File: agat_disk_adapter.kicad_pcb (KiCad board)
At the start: 2 copper layers, 58.4 x 63.5 mm, 14 parts, among them J1 КОНТРОЛЛЕР, J2_A1 ИЗОТ, J2_B2 ИЗОТ, J3 DISK II, J4 GOTEK, J5 Питание GOTEK, J6 ВБ, J7 Джамперы, J8 ВБ2, J9_A1 КОНТРОЛЛЕР, J9_B2 КОНТРОЛЛЕР

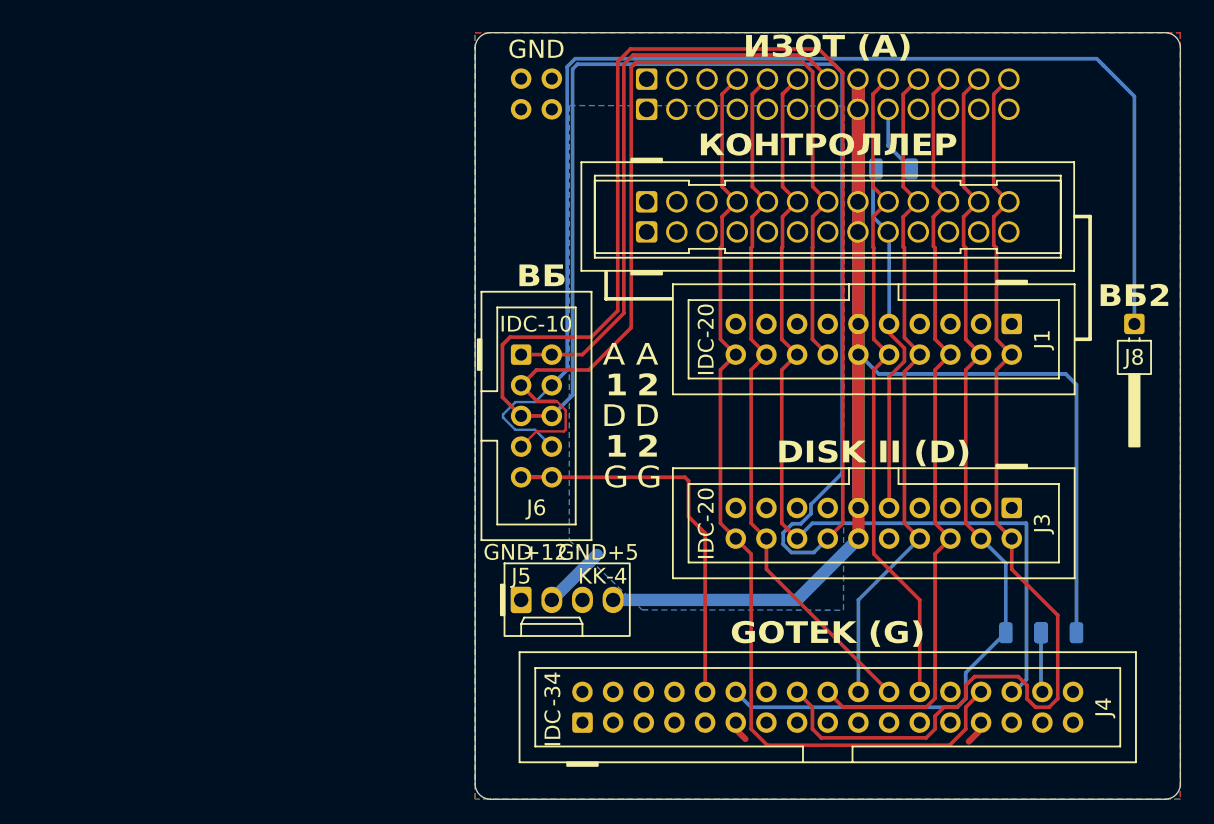
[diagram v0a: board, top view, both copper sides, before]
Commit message: add second FDC connector - Eltra male for standard Agat FDD cable
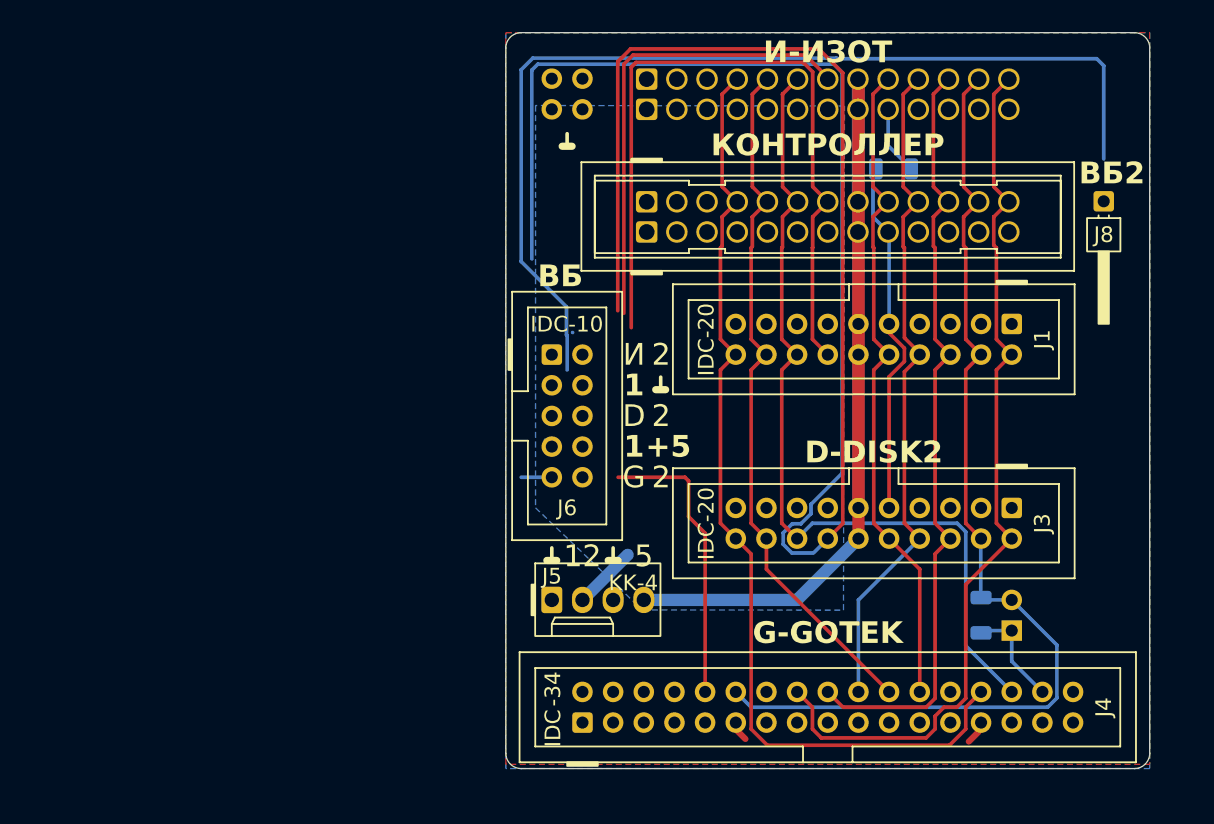
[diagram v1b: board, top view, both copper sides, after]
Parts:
- removed the R2 at (87.7, 89.1)
- added J9: PIN_32, Connector_PinHeader_2.54mm:PinHeader_1x02_P2.54mm_Horizontal, B.Cu at (83.8, 88.9)
- moved J8 10.5 mm to (91.4, 53.3)
- moved R2 3.80 mm to (81.3, 87.6), turned to -90 degrees
- moved J5 2.54 mm to (45.7, 86.4)
- moved J6 2.54 mm to (45.7, 66.0)
- moved J7 2.54 mm to (45.7, 43.2)
- renumbered R3 to R2
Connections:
- net Net-(J4-Pin_32) renamed /PIN_32
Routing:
- net /DS2: track 106.3 -> 0.00 mm
- net /EN1: track 83.6 -> 145.9 mm
- net /+5: track 147.4 -> 105.4 mm
- net /EN_J3: track 200.2 -> 167.5 mm
- net /PH0: track 86.4 -> 75.4 mm
- net /EN_J2: track 48.6 -> 38.6 mm
- net /PH1: track 76.6 -> 85.8 mm
- net /EN_J4: track 34.6 -> 26.6 mm
- net /RD: track 75.1 -> 70.9 mm
- net /PIN_32: track 4.97 -> 9.23 mm
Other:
- board size 58.4 x 63.5 mm -> 53.3 x 61 mm
- board text added: "12"
- board text added: "5"
- board text added: "D-DISK2"
- board text added: "EN1"
- board text added: "EN2"
- board text added: "EN_"
- board text added: "EN_J2"
- board text added: "EN_J3"
- board text added: "EN_J4"
- board text added: "G-GOTEK"
- board text added: "PH0"
- board text added: "PH2"
- board text added: "PH3"
- board text added: "И"
- board text added: "И-ИЗОТ"
- board text added: "КИБЕР- -МУЗЕЙ МУРОМ"
- board text removed: "A"
- board text removed: "DISK II (D)"
- board text removed: "DS1"
- board text removed: "DS2"
- board text removed: "DS_"
- board text removed: "DS_J2"
- board text removed: "DS_J3"
- board text removed: "DS_J4"
- board text removed: "F0"
- board text removed: "F1"
- board text removed: "F2"
- board text removed: "F3"
- board text removed: "GOTEK (G)"
- board text removed: "HTTP://MUSEUM.COMPUTER/"
- board text removed: "ИЗОТ (A)"
- board text removed: "КИБЕР- -МУЗЕЙ МУРОМ 2026"

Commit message: set clearance to 0.22, adjust all traces, align J5 "fan", add J10 "-12->DE2"
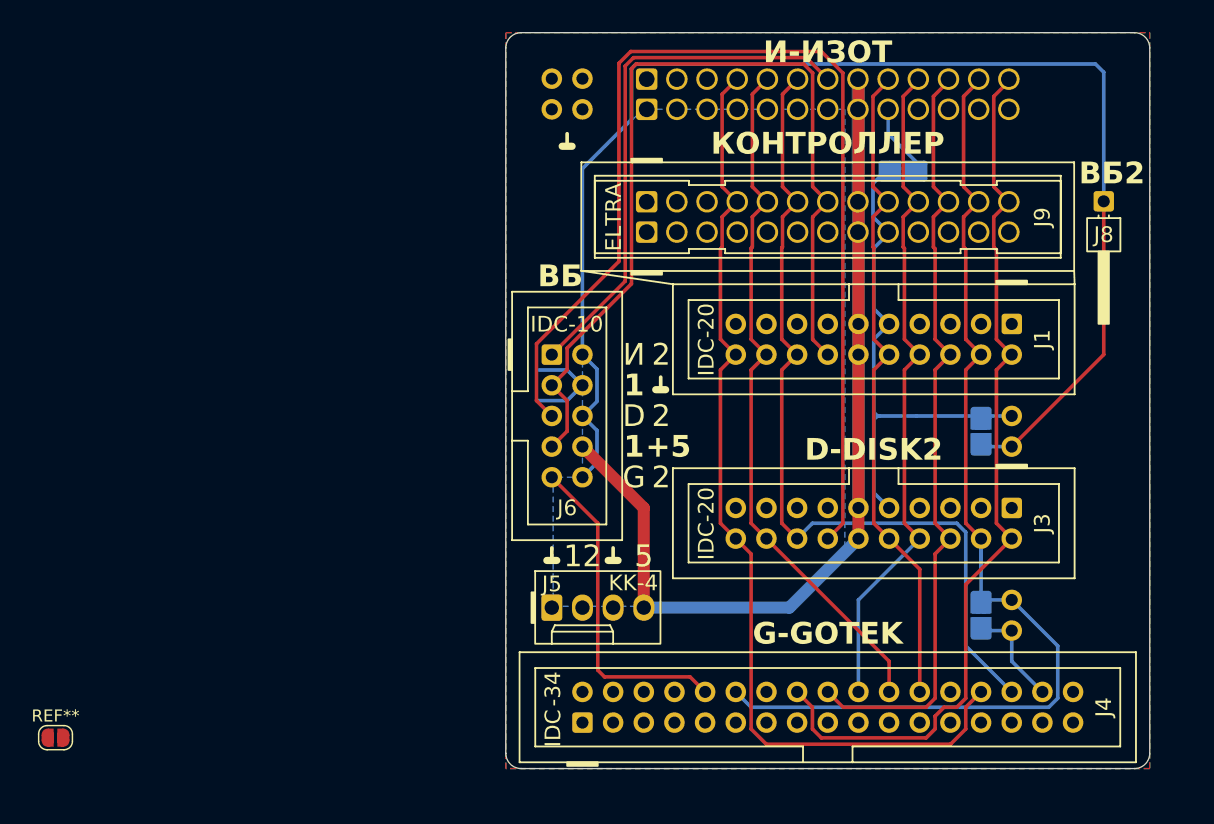
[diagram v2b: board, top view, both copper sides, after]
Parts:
- added J10: PIN_32, Connector_PinHeader_2.54mm:PinHeader_1x02_P2.54mm_Horizontal, B.Cu at (83.8, 73.7)
- added R3: 0, Resistor_SMD:R_1206_3216Metric, B.Cu at (81.3, 72.4)
- added REF**: SolderJumper-2_P1.3mm_Open_RoundedPad1.0x1.5mm, Jumper:SolderJumper-2_P1.3mm_Open_RoundedPad1.0x1.5mm, F.Cu at (4.61, 97.8)
- moved R1 0.80 mm to (74.8, 50.8)
- moved J5 0.64 mm to (45.7, 87.0)
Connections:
- net /EN1 renamed /DE1
- net /PIN_32 renamed /G32
- J2_B2 pad 7: /EN_J2 -> /DE_J2
- J3 pad 14: /EN_J3 -> /DE_J3
- J4 pad 10: /EN_J4 -> /DE_J4
- J6 pad 1: /EN_J2 -> /DE_J2
- J6 pad 10: /EN_J4 -> /DE2
- J6 pad 2: /EN_J2 -> /DE2
- J6 pad 4: /EN2 -> GND
- J6 pad 5: /EN_J3 -> /DE_J3
- J6 pad 6: /EN_J3 -> /DE2
- J6 pad 8: /EN2 -> /+5
- J6 pad 9: /EN_J4 -> /DE_J4
- J8 pad 1: /DS2 -> /DE2
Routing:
- net /EN_J3: track 167.5 -> 0.00 mm
- net /DE2: track 0.00 -> 113.9 mm
- net /DE_J3: track 0.00 -> 91.4 mm
- net /DE1: track 145.9 -> 75.5 mm
- net /DE_J2: track 0.00 -> 44.2 mm
- net /EN_J2: track 38.6 -> 0.00 mm
- net /DE_J4: track 0.00 -> 27.2 mm
- net /EN_J4: track 26.6 -> 0.00 mm
- net /+5: track 105.4 -> 120.6 mm
- net /-12: track 29.1 -> 43.9 mm
- net /+12: track 7.66 -> 0.00 mm
- net GND: track 2.49 -> 8.76 mm
- net /PH1: track 85.8 -> 88.4 mm
- net /PH0: track 75.4 -> 74.5 mm
- net /WRP: track 80.8 -> 80.2 mm
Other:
- board text added: "DE"
- board text added: "DE2"
- board text added: "DE_"
- board text added: "ELTRA"
- board text added: "PH0->GOTEK.32 (fw 307)"
- board text added: "x"
- board text added: "КИБЕР МУЗЕЙ МУРОМ"
- board text removed: "0"
- board text removed: "EN1"
- board text removed: "EN2"
- board text removed: "EN_"
- board text removed: "EN_J2"
- board text removed: "EN_J3"
- board text removed: "EN_J4"
- board text removed: "KEY"
- board text removed: "КИБЕР- -МУЗЕЙ МУРОМ"

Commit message: add solder drop jumper footprint; add led resistor; thermal-relief +5 trace
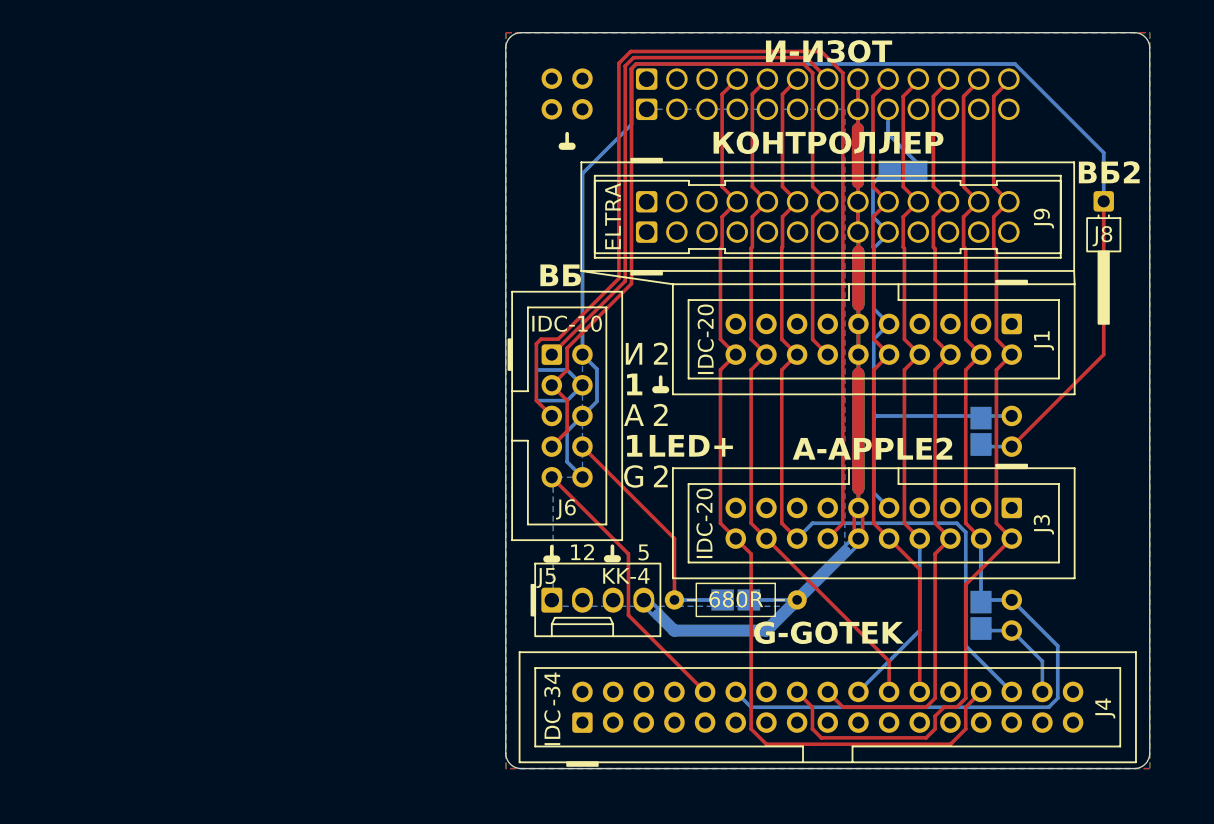
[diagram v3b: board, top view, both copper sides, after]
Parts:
- removed REF**: SolderJumper-2_P1.3mm_Open_RoundedPad1.0x1.5mm, Jumper:SolderJumper-2_P1.3mm_Open_RoundedPad1.0x1.5mm
- added R4: 680R, Resistor_THT:R_Axial_DIN0207_L6.3mm_D2.5mm_P10.16mm_Horizontal, F.Cu at (55.9, 86.4)
- added R5: 680R, agat_disk_adapter:0R_1206_solder_drop_jumper, B.Cu at (61.0, 86.4)
- J3: value DISK II -> IDC‐20
- R1: footprint Resistor_SMD:R_1206_3216Metric -> agat_disk_adapter:0R_1206_solder_drop_jumper
- R2, R3: value 0 -> 0R; footprint Resistor_SMD:R_1206_3216Metric -> agat_disk_adapter:0R_1206_solder_drop_jumper
- moved J5 0.62 mm to (45.7, 86.4)
- turned R2 to 90 degrees
- turned R3 to 90 degrees
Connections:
- J1 pad 9: /-12 -> /-12|DE2
- J10 pad 2: /-12 -> /-12|DE2
- J3 pad 9: /-12 -> /-12|DE2
- J6 pad 8: /+5 -> /LED+
- J9_A1 pad 9: /-12 -> /-12|DE2
- R1 pad 2: /-12 -> /-12|DE2
- R2 pad 1: /PH1 -> /G32
- R2 pad 2: /G32 -> /PH1
- R3 pad 1: /-12 -> /DE2
- R3 pad 2: /DE2 -> /-12|DE2
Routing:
- net /-12: track 43.9 -> 0.00 mm
- net /-12|DE2: track 0.00 -> 42.4 mm
- net /LED+: track 0.00 -> 19.5 mm
- net /+5: track 120.6 -> 105.6 mm
- net /DE_J4: track 27.2 -> 23.0 mm
- net /DE2: track 113.9 -> 110.2 mm
- net /DE_J3: track 91.4 -> 92.2 mm
- net /G32: track 9.23 -> 8.67 mm
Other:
- board text added: "A"
- board text added: "A-APPLE2"
- board text added: "LED+"
- board text added: "КИБЕР‐ МУЗЕЙ МУРОМ"
- board text removed: "D"
- board text removed: "D-DISK2"
- board text removed: "KK‐4"
- board text removed: "КИБЕР МУЗЕЙ МУРОМ"

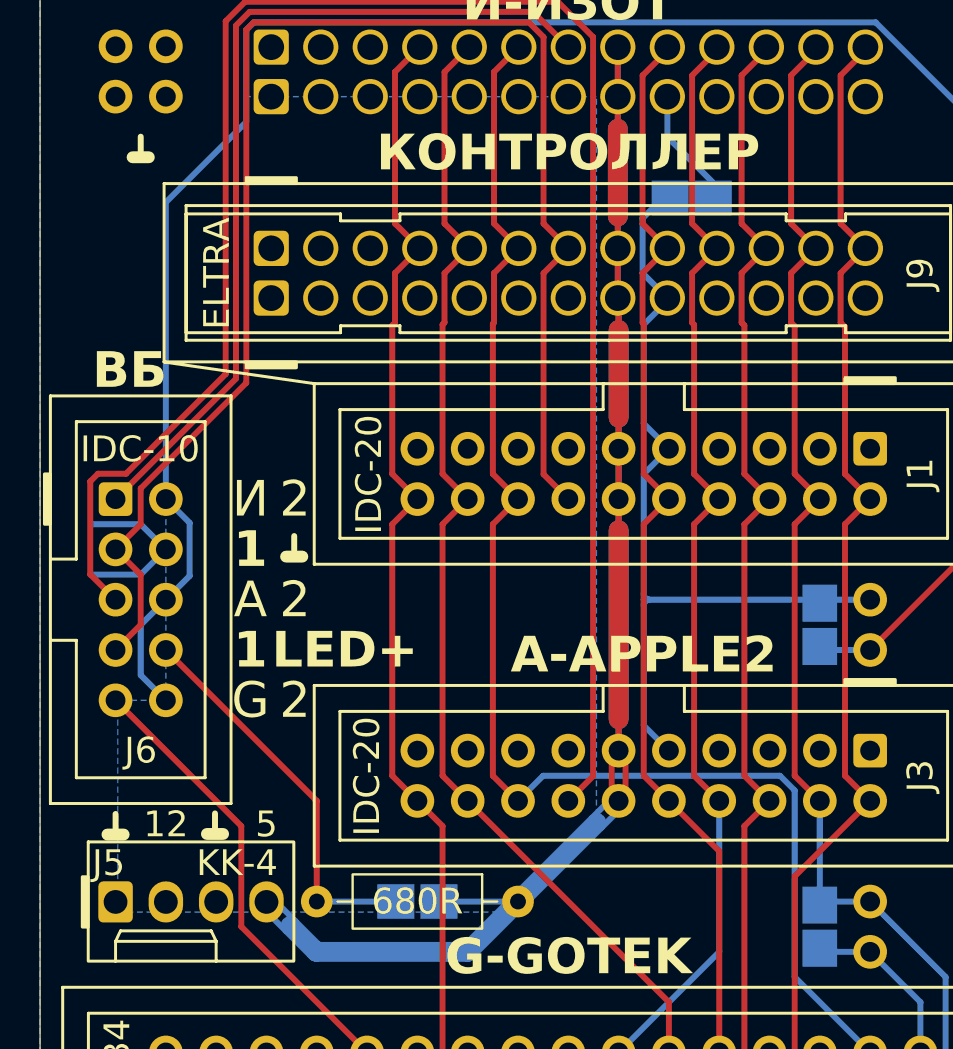
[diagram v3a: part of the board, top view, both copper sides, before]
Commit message: flip front panel DE connector for better tracing
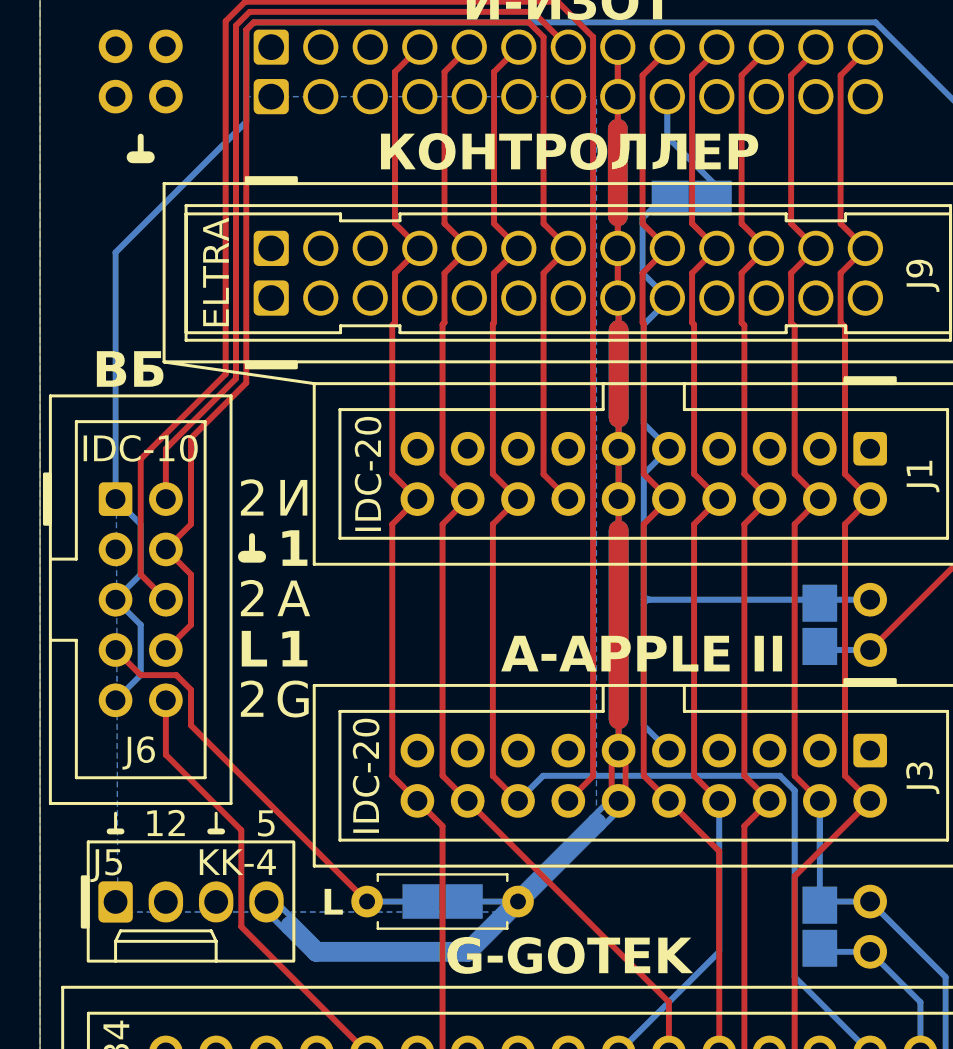
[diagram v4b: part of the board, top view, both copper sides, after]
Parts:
- R4: footprint Resistor_THT:R_Axial_DIN0207_L6.3mm_D2.5mm_P10.16mm_Horizontal -> Resistor_THT:R_Axial_DIN0207_L6.3mm_D2.5mm_P7.62mm_Horizontal
- moved R4 2.54 mm to (58.4, 86.4)
- moved R5 1.27 mm to (62.2, 86.4)
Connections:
- J6 pad 1: /DE_J2 -> /DE2
- J6 pad 10: /DE2 -> /DE_J4
- J6 pad 2: /DE2 -> /DE_J2
- J6 pad 3: /DE1 -> GND
- J6 pad 4: GND -> /DE1
- J6 pad 5: /DE_J3 -> /DE2
- J6 pad 6: /DE2 -> /DE_J3
- J6 pad 7: /DE1 -> /LED+
- J6 pad 8: /LED+ -> /DE1
- J6 pad 9: /DE_J4 -> /DE2
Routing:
- net GND: track 8.76 -> 0.11 mm
- net /LED+: track 19.5 -> 21.7 mm
- net /DE_J3: track 92.2 -> 90.3 mm
- net /DE2: track 110.2 -> 111.3 mm
- net /DE_J4: track 23.0 -> 22.0 mm
- net /DE1: track 75.5 -> 74.4 mm
- net /DE_J2: track 44.2 -> 43.2 mm
- net /+5: track 105.6 -> 104.7 mm
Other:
- board text added: "A-APPLE II"
- board text added: "L"
- board text removed: "A-APPLE2"
- board text removed: "DE"
- board text removed: "LED+"
